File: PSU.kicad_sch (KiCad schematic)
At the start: 56 parts, among them U11 TPSM84338, U13 TPS26400PWPR, U14 TPS7A39, U18 TLV1117-33

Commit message: modified:   MCU.kicad_sch 	modified:   PSU.kicad_sch 	modified:   ProjectY.kicad_pro 	modified:   ProjectY.kicad_sch 	modified:   ad.kicad_sch 	modified:   audio.kicad_sch
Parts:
- removed C22, C48, C69, C71: C, symbol Device:C
- removed C41, C42: ?, symbol Device:C_Small
- removed C70: ?, symbol Device:C_Polarized
- removed C81: ?, symbol Device:C
- removed C82, C83, C84, C85, C86: 10u, symbol Device:C
- removed L6: L, symbol Device:L
- removed R39, R40, R63: ?, symbol Device:R_Small
- removed R47: 680k, symbol Device:R
- removed R50: ?, symbol Device:R
- removed R61: 54.9k, symbol Device:R_Small
- removed R62, R64: 10k, symbol Device:R_Small
- removed R68: 0, symbol Device:R_Small
- removed U11: TPSM84338, symbol User:TPSM84338_
- removed U14: TPS7A39, Package_SON:Texas_S-PVSON-N10_ThermalVias, symbol Regulator_Linear:TPS7A39
- added U11: RT8293B, symbol User:RT8293B
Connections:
- net GND: now also U11.4 (GND), U11.9 (GND)
- no-connect marks 5 -> 4
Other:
- note added: "RT8293AHZSP"
- moved on the sheet: C52, C53, C54, L2, R54, R55

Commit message: modified:   MCU.kicad_sch 	modified:   PSU.kicad_sch 	modified:   ProjectY.kicad_pro 	modified:   ProjectY.kicad_sch 	modified:   audio.kicad_sch 	modified:   fp-info-cache 	new file:   spdif.kicad_sch 	modified:   usbfilter.kicad_sch
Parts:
- removed C53, C58: ?, symbol Device:C_Polarized
- removed C56: Css, symbol Device:C_Polarized_Small
- removed C57: C, symbol Device:C
- removed C79, C80: 10u, symbol Device:C
- removed D1: D_TVS, symbol Device:D_TVS
- removed L3: Choke_Wurth_WE-CNSW_744232090, Inductor_SMD:L_CommonMode_Wurth_WE-CNSW-1206, symbol Filter:Choke_Wurth_WE-CNSW_744232090
- removed L4: L, symbol Device:L
- removed R54, R55, R60: 0, symbol Device:R_Small
- removed R57, R58, R59: ?, symbol Device:R_Small
- removed U13: TPS26400PWPR, PWP0016H-IPC_A, symbol 2025-02-23_17-32-12:TPS26400PWPR
- removed U18: TLV1117-33, symbol Regulator_Linear:TLV1117-33
- added C3, C4, C5, C6, C7, C9: 10uF, PCM_JLCPCB:C_0603, symbol PCM_JLCPCB-Capacitors:0603,10uF,(2)
- added C49: C, symbol Device:C
- added D1: 1N4148W, PCM_JLCPCB:D_SOD-123, symbol PCM_JLCPCB-Diodes:Switching,1N4148W
- added FB1, FB2: FerriteBead, symbol Device:FerriteBead
- added L1: Choke_Wurth_WE-CNSW_744232090, Inductor_SMD:L_CommonMode_Wurth_WE-CNSW-1206, symbol Filter:Choke_Wurth_WE-CNSW_744232090
- added R10, R11: 5.1kΩ, PCM_JLCPCB:R_0402, symbol PCM_JLCPCB-Resistors:0402,5.1kΩ
- added R12: 0Ω, PCM_JLCPCB:R_0402, symbol PCM_JLCPCB-Resistors:0402,0Ω
- added U12: USBLC6-2P6, Package_TO_SOT_SMD:SOT-666, symbol Power_Protection:USBLC6-2P6
- added U4: TPS7A39, Package_SON:Texas_S-PVSON-N10_ThermalVias, symbol Regulator_Linear:TPS7A39
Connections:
- net +3.3V: now also C50.1, FB3.1, R48.1, TP1.1, U11.5 (FB); no longer C51.1, FB3.2, R56.1
- net +9V: now also C3.1, C4.1, C5.1, C6.1, C7.1, C9.1
- net GND: now also C3.2, C4.2, C49.2, C5.2, C6.2, C7.2, C9.2, R10.1, R11.1, U12.2 (GND)
- net at U11.2 (VIN): now also L2.2
- net at C52.1: now also R12.2
- net +9V_protected: no longer names the net of C54.1, L2.1
- new net: C51.1, FB3.2, R56.1
- new net: L1.2, U12.1 (I/O1)
- new net: L1.3, U12.3 (I/O2)
- new net: D1.2, FB2.2
- new net: U4.11 (GND), U4.4 (GND)
- new net: C49.1, FB1.2, FB2.1
- new net CC: R10.2
- new net D+: U12.6 (I/O1)
- new net D-: U12.4 (I/O2)
- new net Dfiltered+: L1.1
- new net Dfiltered-: L1.4
- new net VBUS: FB1.1, U12.5 (VBUS)
- new net VBUS_detect: D1.1
- new net VCONN: R11.2
- no-connect marks 4 -> 0
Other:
- note added: "4-18V"
- note added: "OR controller"
- note added: "TPS65133"
- note removed: "RT8293AHZSP"
- moved on the sheet: C24, C50, C51, C52, C54, C55, FB3, L2, R48, R49, R51, R56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

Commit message: asd
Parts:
- removed C24: ?, symbol Device:C_Small
- removed C3, C4, C5, C6, C7: 10uF, PCM_JLCPCB:C_0603, symbol PCM_JLCPCB-Capacitors:0603,10uF,(2)
- removed C49: C, symbol Device:C
- removed D1: 1N4148W, PCM_JLCPCB:D_SOD-123, symbol PCM_JLCPCB-Diodes:Switching,1N4148W
- removed FB1, FB2: FerriteBead, symbol Device:FerriteBead
- removed R48: 50, symbol Device:R_Small
- removed R49: ?, symbol Device:R_Small
- removed R51: 10k, symbol Device:R_Small
- removed TP1: 3.3V, symbol Connector:TestPoint
- removed TP2: Bode100, symbol Connector:TestPoint
- added C14, C64: 10uF, PCM_JLCPCB:C_0603, symbol PCM_JLCPCB-Capacitors:0603,10uF,(2)
- added C24: DNP, Capacitor_SMD:C_0805_2012Metric, symbol Device:C
- added C25, C58, C59, C60, C61, C62, C68, C69: 10uF, PCM_JLCPCB:C_0402, symbol PCM_JLCPCB-Capacitors:0402,10uF
- added C26, C33, C41, C42, C48, C49, C5, C6, C7: 10uF, PCM_JLCPCB:C_0603, symbol PCM_JLCPCB-Capacitors:0603,10uF
- added C3, C4, C57: 100nF, PCM_JLCPCB:C_0402, symbol PCM_JLCPCB-Capacitors:0402,100nF,(2)
- added C53, C56: 100uF, PCM_JLCPCB:C_CASE-B-3528-21(mm), symbol PCM_JLCPCB-Capacitors:CASE-B-3528-21(mm),100uF
- added C63: 2.2nF, PCM_JLCPCB:C_0805, symbol PCM_JLCPCB-Capacitors:0805,2.2nF
- added C65, C66, C67: C, symbol Device:C
- added D1: SMF20CA, PCM_JLCPCB:D_SOD-123FL, symbol PCM_JLCPCB-Diodes:TVS-Uni,SMF20CA
- added L3: 3.6uH, symbol Device:L
- added L4, L5: XFL4020-472MEC, Inductor_SMD:L_Coilcraft_XxL4020, symbol Device:L
- added Q1: DMT6008LFG, Package_SON:Diodes_PowerDI3333-8, symbol Transistor_FET:DMT6008LFG
- added R36: 4.7kΩ, PCM_JLCPCB:R_0402, symbol PCM_JLCPCB-Resistors:0402,4.7kΩ
- added R39, R57, R58, R60: 10kΩ, PCM_JLCPCB:R_0402, symbol PCM_JLCPCB-Resistors:0402,10kΩ
- added R46: 22kΩ, PCM_JLCPCB:R_0402, symbol PCM_JLCPCB-Resistors:0402,22kΩ
- added R47: 47kΩ, PCM_JLCPCB:R_0402, symbol PCM_JLCPCB-Resistors:0402,47kΩ
- added R48, R51, R53, R55: 4.7kΩ, PCM_JLCPCB:R_0603, symbol PCM_JLCPCB-Resistors:0603,4.7kΩ
- added R49, R50, R52, R54, R59, R61: R, symbol Device:R
- added U17: TPS2121RUXR, User:IC_TPS2121RUXR, symbol User:TPS2121RUXR
- added U19: TLV77333PDBVR, Package_TO_SOT_SMD:SOT-23-5, symbol Regulator_Linear:AP2127K-3.3
- added U20: TPS65133DPDR, User:SON40P300X300X80-13N, symbol User:TPS65133DPDR
- added U21: LM74700, Package_TO_SOT_SMD:SOT-23-6, symbol Power_Management:LM74700
- added U22: TLV77325PDBVR, Package_TO_SOT_SMD:SOT-23-5, symbol Regulator_Linear:AP2127K-3.3
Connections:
- net GND is gone; now on net AGND: C50.2, C51.2, C52.2, C54.2, C55.2, C9.2, R10.1, R11.1, U11.4 (GND), U11.9 (GND), U12.2 (GND)
- net +3.3V: now also C58.1, C59.1, C60.1, C61.1, C62.1, C68.1, L3.2, R57.1, U22.1 (VIN), U22.3 (EN); no longer U11.5 (FB)
- net +9V: now also C3.1, C4.1, D1.1, Q1.1 (S), Q1.2 (S), Q1.3 (S), U21.3 (EN), U21.6 (ANODE); no longer C9.1
- net VBUS: now also C14.2, R36.1, R52.1, R54.1, U17.2 (IN2), U17.2_1 (IN2__1)
- net VIN_FILT: now reaches R12.1
- net VIN_FILT: now also L2.2, U11.2 (VIN), C65.1
- net AVIN: now reaches C51.1, FB3.2, R56.1
- net AVIN: now also L5.2, U20.11 (AVIN), U20.12 (PVIN), U20.7 (EN)
- net at U11.1 (BOOT): now also C57.1
- net at U11.3 (SW): now also C57.2, L3.1
- net at U11.6 (COMP): now also C24.1, R46.1
- net VIN_4V-18V: now reaches C54.1, L2.1
- net VIN_4V-18V: now also U17.1 (OUT), U17.1_1 (OUT__1), U17.8 (OUT__2), U17.8_1 (OUT__3)
- net +5V: now reaches U4.1 (INP)
- net +5V: now also U4.2 (EN), C26.1, C41.1, C48.1, C5.1, C6.1, U19.1 (VIN), U19.3 (EN), U20.3 (VPOS)
- net +4.5V: now reaches U4.10 (OUTP)
- net +4.5V: now also C53.1, C66.1, R59.1
- net AGND: now reaches U4.11 (GND), U4.4 (GND)
- net AGND: now also C14.1, C24.2, C25.2, C26.2, C3.2, C33.1, C41.2, C42.1, C48.2, C49.1, C5.2, C53.2, C56.1, C58.2, C59.2, C6.2, C60.2, C61.2, C62.2, C63.2, C64.2, C65.2, C68.2, C69.2, C7.1, D1.2, L4.1, R39.2, R47.2, R48.2, R51.2, R53.2, R55.2, R58.2, U17.12 (GND), U19.2 (GND), U19.4 (NC), U20.13 (EP), U20.2 (PGND), U20.4 (GND), U20.5 (AGND), U20.6 (GND__1), U20.8 (GND__2), U21.2 (GND), U22.2 (GND), U22.4 (NC)
- net -5V: now reaches U4.5 (INN)
- net -5V: now also C33.2, C42.2, C49.2, C7.2, U20.9 (VNEG)
- net -4.5V: now reaches U4.6 (OUTN)
- net -4.5V: now also C56.2, C67.2, R61.2
- net FBN: now reaches U4.7 (FBN)
- net FBN: now also C67.1, R60.2, R61.1
- net BUF: now reaches U4.8 (BUF)
- net BUF: now also R60.1
- net FBP: now reaches U4.9 (FBP)
- net FBP: now also C66.2, R58.1, R59.2
- new net: R52.2, R53.1, U17.4 (OV2)
- new net: L4.2, U20.10 (SWN)
- new net: C4.2, U21.1 (VCAP)
- new net: Q1.4 (G), U21.5 (GATE)
- new net: R50.2, R51.1, U17.5 (OV1)
- new net: C63.1, R46.2
- new net: L5.1, U20.1 (SWP)
- new net: R47.1, U17.10 (ILIM)
- new net: C64.1, U17.11 (SS)
- new net +2.5VA: C69.1, U22.5 (VOUT)
- new net +3.3VA: C25.1, U19.5 (VOUT)
- new net +9V_REVERSE_PROTECTED: C9.1, Q1.5 (D), R49.1, R50.1, U17.7 (IN1), U17.7_1 (IN1__1), U21.4 (CATHODE)
- new net CP2: R54.2, R55.1, U17.3 (CP2)
- new net PR1: R48.1, R49.2, U17.6 (PR1)
- new net PSU_ST: R57.2, U17.9 (ST)
- new net VBUS_DETECT: R36.2, R39.1
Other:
- note removed: "4-18V"
- note removed: "OR controller"
- note removed: "TPS65133"
- moved on the sheet: C50, C51, C52, C54, C55, C9, FB3, L2, R12, R56, U11, U4

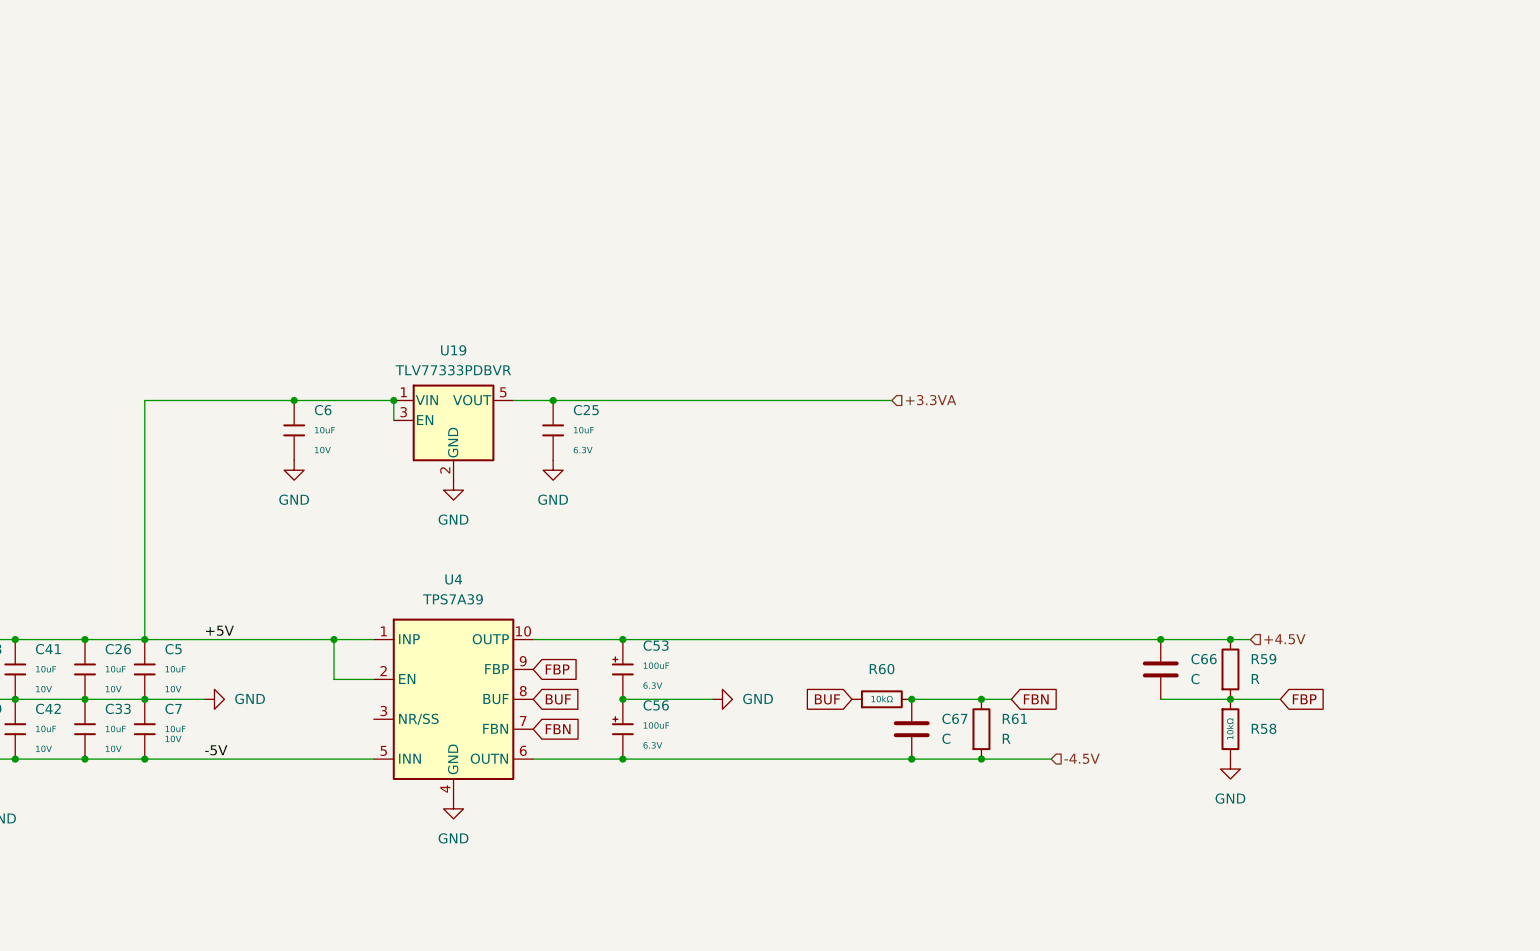
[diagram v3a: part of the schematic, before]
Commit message: added decoupling for DSP
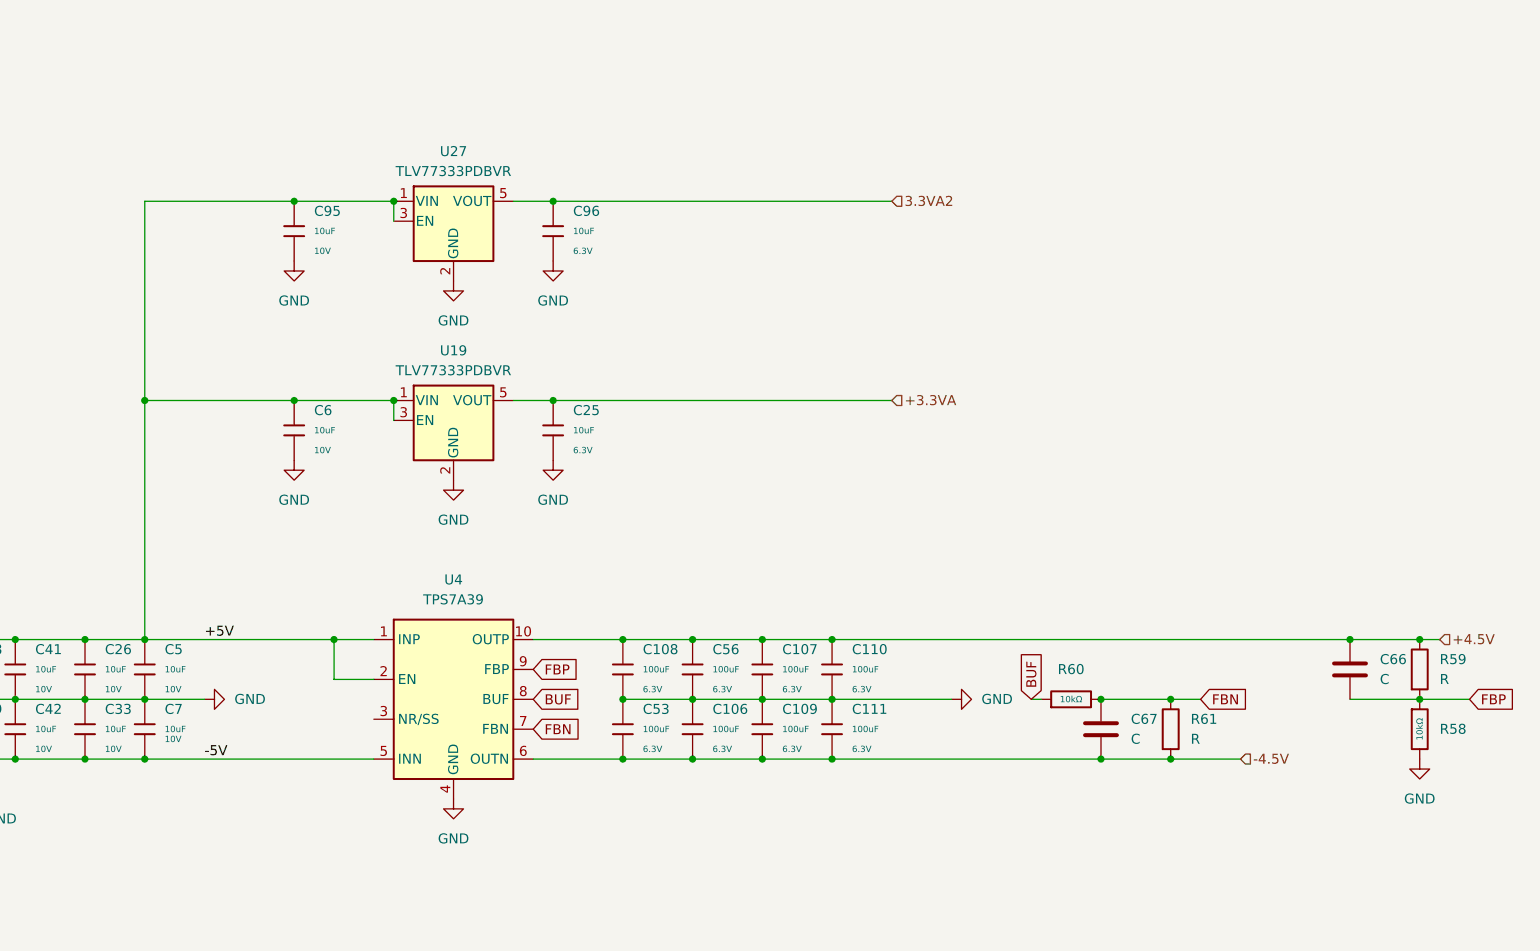
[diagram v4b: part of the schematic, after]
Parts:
- removed C53, C56: 100uF, PCM_JLCPCB:C_CASE-B-3528-21(mm), symbol PCM_JLCPCB-Capacitors:CASE-B-3528-21(mm),100uF
- added C106, C107, C108, C109, C110, C111, C53, C56: 100uF, PCM_JLCPCB:C_1206, symbol PCM_JLCPCB-Capacitors:1206,100uF
- added C95: 10uF, PCM_JLCPCB:C_0603, symbol PCM_JLCPCB-Capacitors:0603,10uF
- added C96: 10uF, PCM_JLCPCB:C_0402, symbol PCM_JLCPCB-Capacitors:0402,10uF
- added U27: TLV77333PDBVR, Package_TO_SOT_SMD:SOT-23-5, symbol Regulator_Linear:AP2127K-3.3
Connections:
- net +4.5V: now also C107.1, C108.1, C110.1, C56.1
- net +5V: now also C95.1, U27.1 (VIN), U27.3 (EN)
- net -4.5V: now also C106.2, C109.2, C111.2, C53.2
- net AGND: now also C106.1, C107.2, C108.2, C109.1, C110.2, C111.1, C53.1, C56.2, C95.2, C96.2, U27.2 (GND), U27.4 (NC)
- new net 3.3VA2: C96.1, U27.5 (VOUT)
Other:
- moved on the sheet: C66, C67, R58, R59, R60, R61

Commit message: started the layout process
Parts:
- removed C6, C95: 10uF, PCM_JLCPCB:C_0603, symbol PCM_JLCPCB-Capacitors:0603,10uF
- removed C66, C67: C, symbol Device:C
- added C6, C78: 10uF, PCM_JLCPCB:C_0402, symbol PCM_JLCPCB-Capacitors:0402,10uF
- added C66, C79: 10nF, PCM_JLCPCB:C_0402, symbol PCM_JLCPCB-Capacitors:0402,10nF
- R59, R61: footprint (none) -> Resistor_SMD:R_0402_1005Metric
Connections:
- net +4.5V: now also C79.1
- net +5V: now also C6.1, C78.1
- net -4.5V: now also C66.2
- net AGND: now also C6.2, C78.2
- net FBN: now also C66.1
- net FBP: now also C79.2

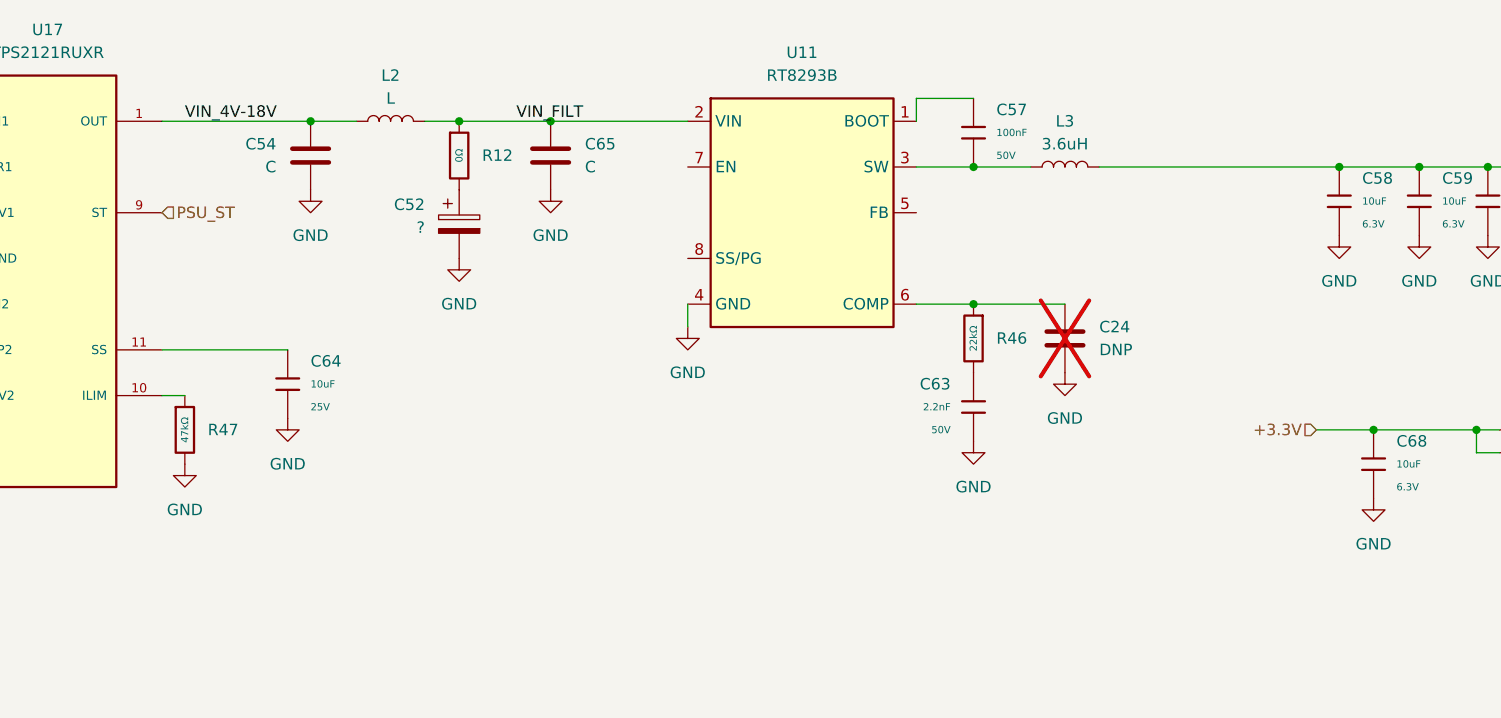
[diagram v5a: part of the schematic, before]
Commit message: 3v3 dcdc update
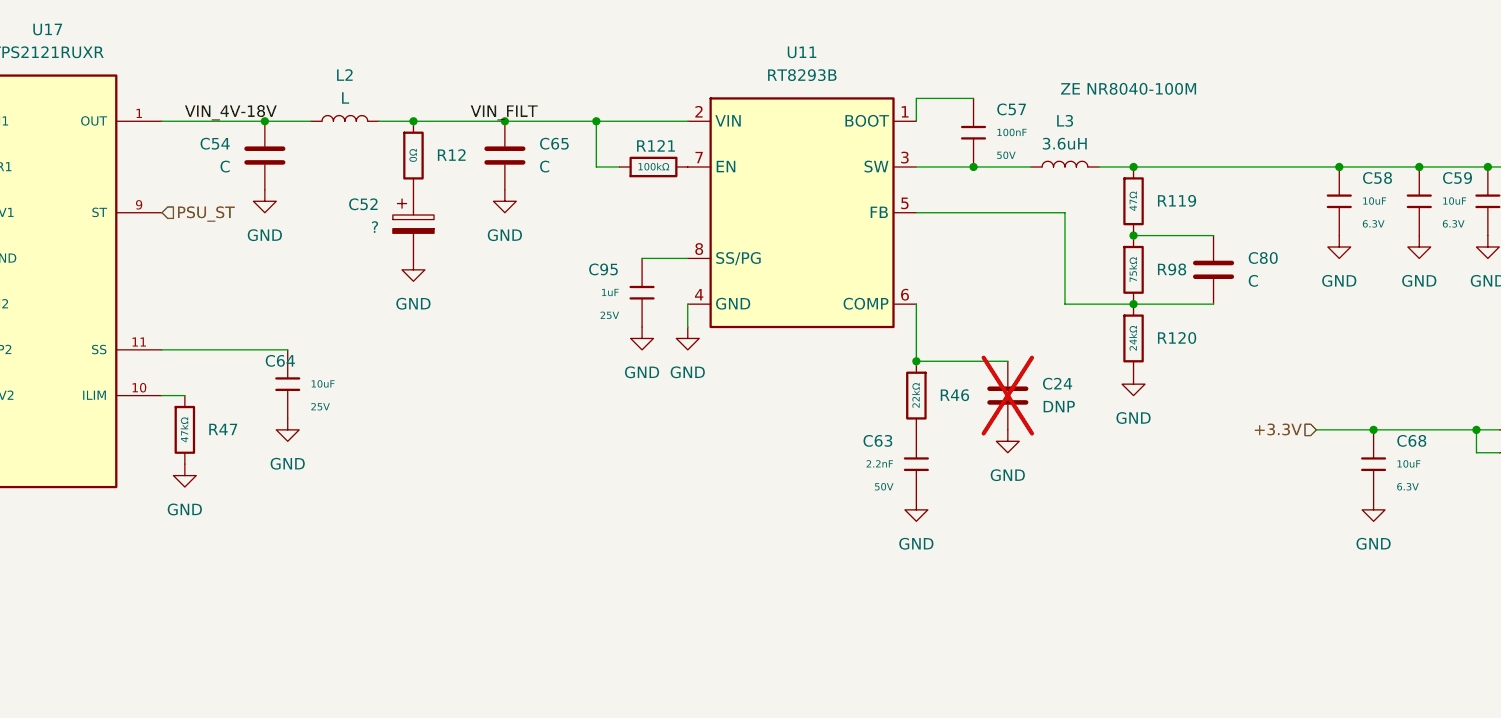
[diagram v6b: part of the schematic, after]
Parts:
- added C80: C, Capacitor_SMD:C_0402_1005Metric, symbol Device:C
- added C95: 1uF, PCM_JLCPCB:C_0402, symbol PCM_JLCPCB-Capacitors:0402,1uF
- added R119: 47Ω, PCM_JLCPCB:R_0402, symbol PCM_JLCPCB-Resistors:0402,47Ω
- added R120: 24kΩ, PCM_JLCPCB:R_0402, symbol PCM_JLCPCB-Resistors:0402,24kΩ
- added R121: 100kΩ, PCM_JLCPCB:R_0402, symbol PCM_JLCPCB-Resistors:0402,100kΩ
- added R98: 75kΩ, PCM_JLCPCB:R_0402, symbol PCM_JLCPCB-Resistors:0402,75kΩ
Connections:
- net +3.3V: now also R119.1
- net AGND: now also C95.2, R120.2
- net VIN_FILT: now also R121.1
- net at U11.5 (FB): now also C80.2, R120.1, R98.2
- net at U11.7 (EN): now also R121.2
- net at U11.8 (SS/PG): now also C95.1
- new net: C80.1, R119.2, R98.1
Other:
- moved on the sheet: C24, C52, C54, C63, C65, L2, R12, R46
